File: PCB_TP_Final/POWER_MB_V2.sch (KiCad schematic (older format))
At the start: 1 part, among them M1 POWER_MB_V2

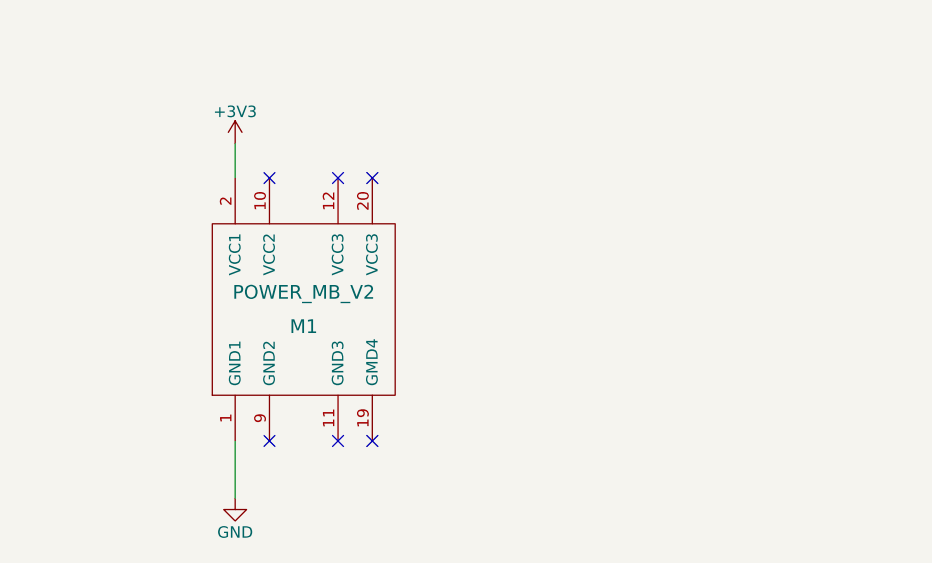
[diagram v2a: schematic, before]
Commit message: Se agregaron correcciones sugeridas
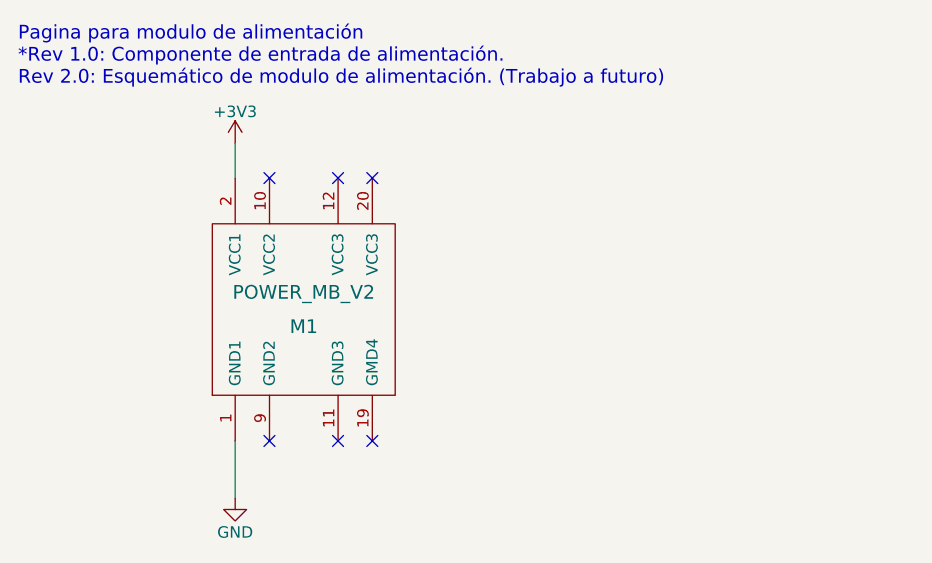
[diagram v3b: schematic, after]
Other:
- note added: "Pagina para modulo de alimentación\n*Rev 1.0: Componente de entrada de alimentación.\nRev 2.0: Esquemático de modulo de alimentación. (Trabajo a futuro)"
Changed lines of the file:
@@
 encoding utf-8
 Sheet 4 5
-Title ""
+Title "Power MB v2"
 Date "2018-09-26"
-Rev ""
-Comp ""
+Rev "1.0"
+Comp "Ericson Joseph Estupiñan Pineda"
 Comment1 ""
 Comment2 ""
@@
 NoConn ~ 6150 4300
 $Comp
-L GND #PWR06
+L GND #PWR09
 U 1 1 5BA7CDDB
 P 5550 4550
-F 0 "#PWR06" H 5550 4300 50  0001 C CNN
+F 0 "#PWR09" H 5550 4300 50  0001 C CNN
 F 1 "GND" H 5550 4400 50  0000 C CNN
 F 2 "" H 5550 4550 50  0001 C CNN
@@
 $EndComp
 $Comp
-L +3V3 #PWR07
+L +3V3 #PWR010
 U 1 1 5BA9BDEF
 P 5550 3000
-F 0 "#PWR07" H 5550 2850 50  0001 C CNN
+F 0 "#PWR010" H 5550 2850 50  0001 C CNN
 F 1 "+3V3" H 5550 3140 50  0000 C CNN
 F 2 "" H 5550 3000 50  0001 C CNN
@@
 	5550 4300 5550 4550
 NoConn ~ 6000 4300
+Text Notes 4600 2750 0    60   ~ 0
+Pagina para modulo de alimentación\n*Rev 1.0: Componente de entrada de alimentación.\nRev 2.0: Esquemático de modulo de alimentación. (Trabajo a futuro)
 $EndSCHEMATC
